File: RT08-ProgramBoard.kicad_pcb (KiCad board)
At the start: 2 copper layers, 309 parts, among them J1 PWR/Addr, J2 Instruction, J3 Data, J4 Instruction, J5 Data

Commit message: Moved a bit, updated things.csv
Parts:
- moved C10 1.27 mm to (99.1, 99.1)
- moved C11 1.27 mm to (144.8, 99.1)
- moved C12 1.27 mm to (190.5, 99.1)
- moved C14 1.27 mm to (99.1, 132.1)
- moved C15 1.27 mm to (144.8, 132.1)
- moved C16 1.27 mm to (190.5, 132.1)
- moved C2 1.27 mm to (99.1, 33.0)
- moved C3 1.27 mm to (144.8, 33.0)
- moved C4 1.27 mm to (190.5, 33.0)
- moved C6 1.27 mm to (99.1, 66.0)
- moved C7 1.27 mm to (144.8, 66.0)
- moved C8 1.27 mm to (190.5, 66.0)
- moved D11 1.27 mm to (96.5, 76.2)
- moved D12 1.27 mm to (96.5, 73.7)
- moved D19 1.27 mm to (96.5, 109.2)
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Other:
- board outline added: 190.5 x 149.9 mm

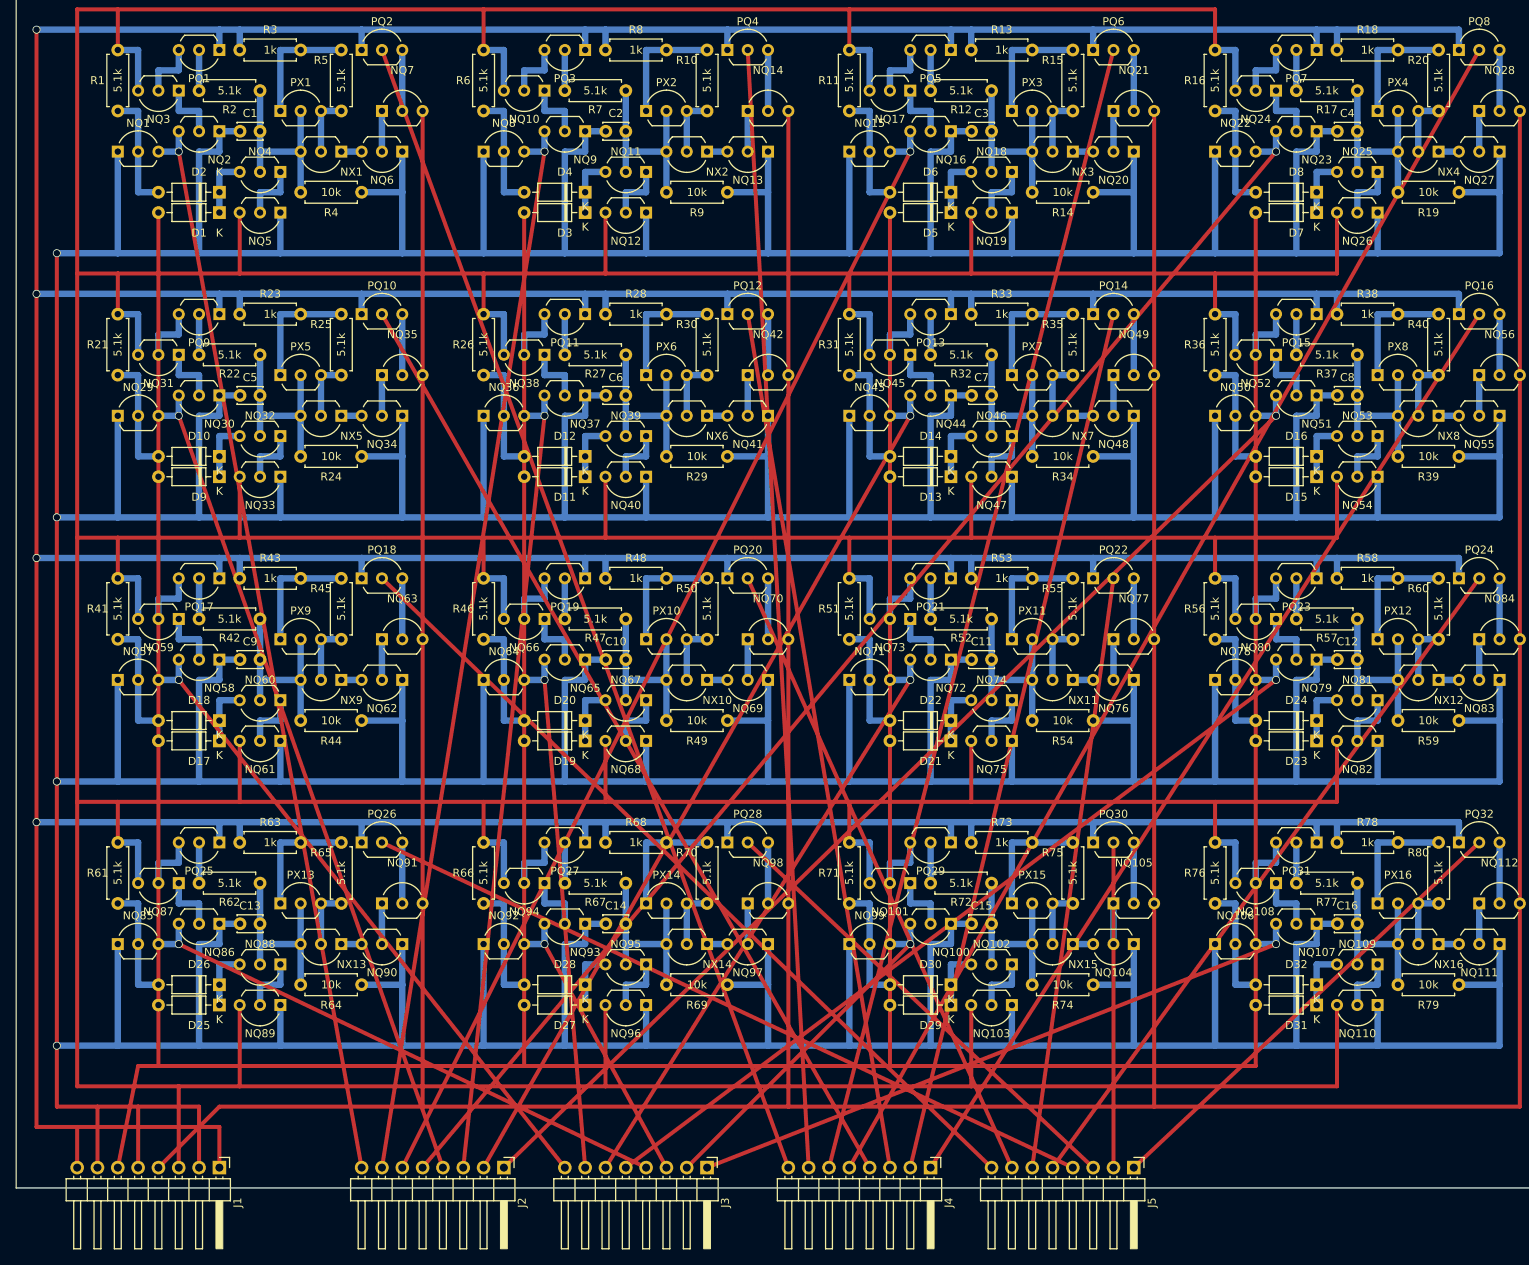
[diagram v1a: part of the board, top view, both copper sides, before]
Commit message: Deleted '-' from its name, officially
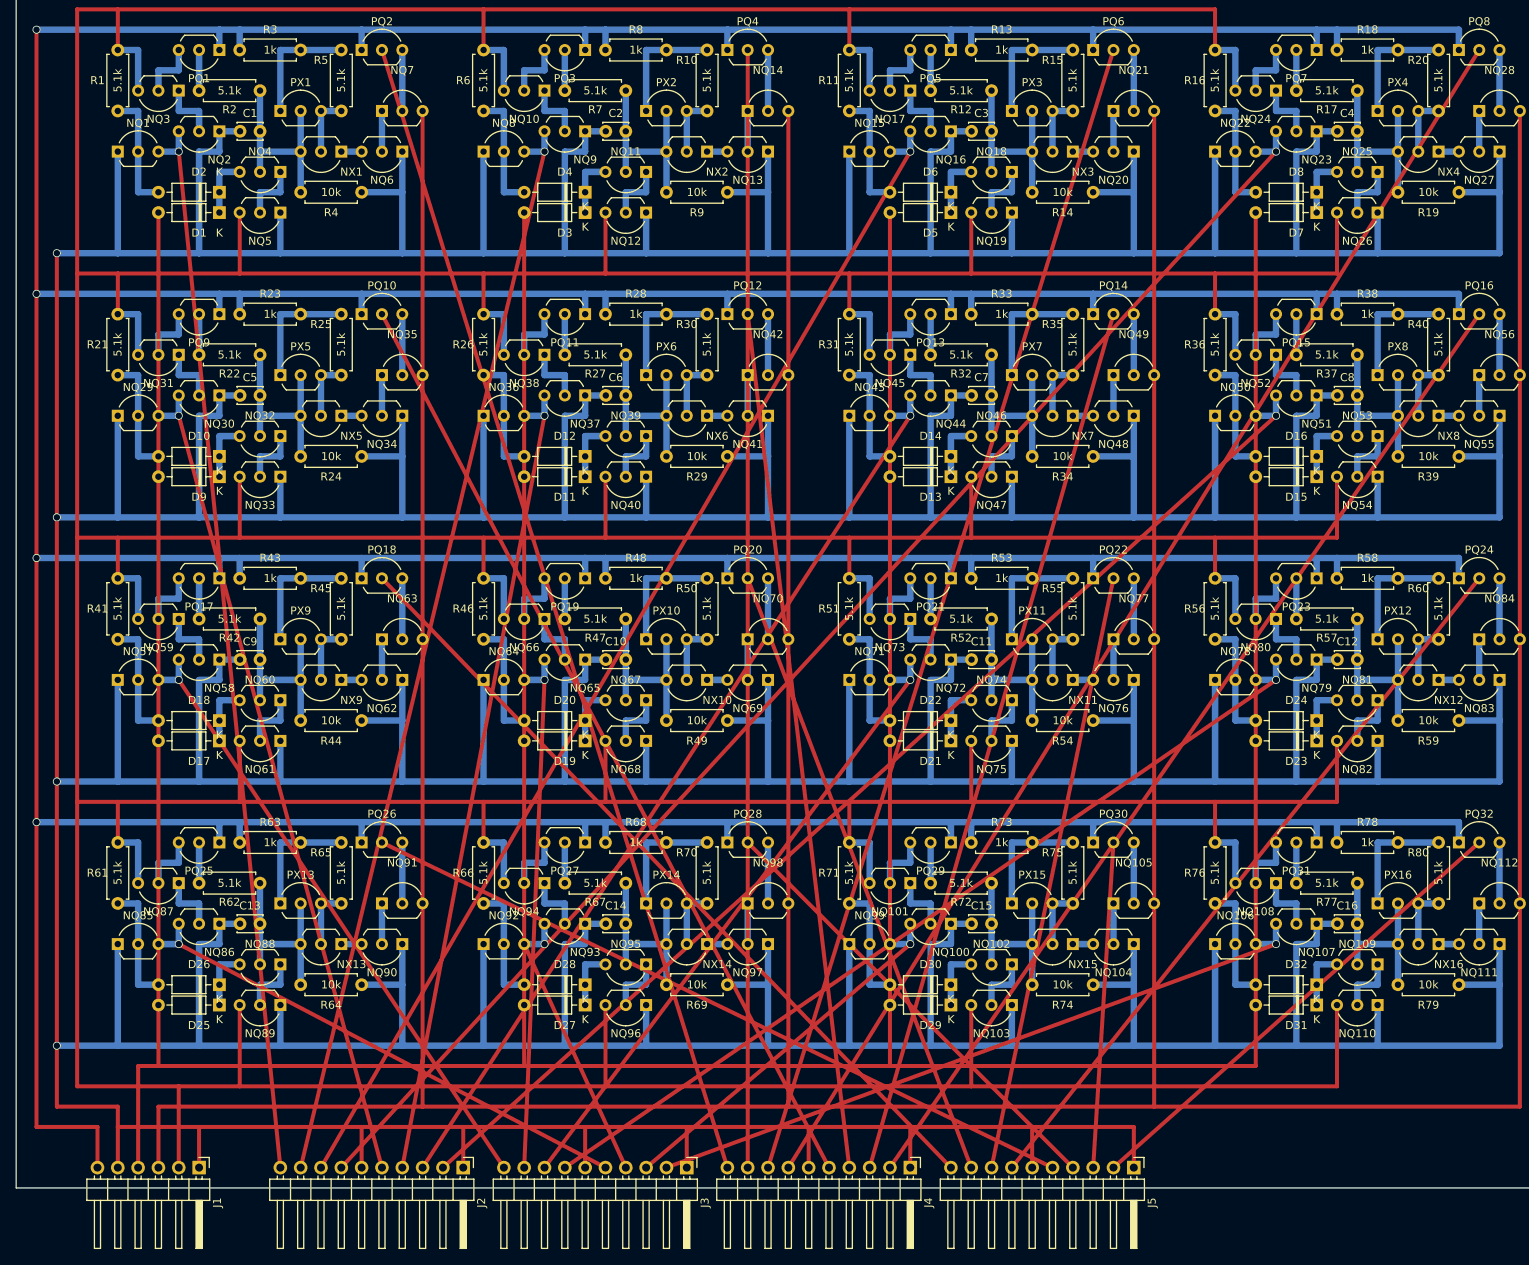
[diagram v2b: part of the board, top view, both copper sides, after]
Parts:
- D1, D10, D11, D12, D13, D14, D15, D16, D17, D18, D19, D2, D20, D21, D22, D23, D24, D25, D26, D27, D28, D29, D3, D30, D31, D32, D4, D5, D6, D7, D8, D9: value 30V0.2A -> Schottky
- J1: footprint Connector_PinHeader_2.54mm:PinHeader_1x08_P2.54mm_Horizontal -> Connector_PinHeader_2.54mm:PinHeader_1x06_P2.54mm_Horizontal
- J2, J3, J4, J5: footprint Connector_PinHeader_2.54mm:PinHeader_1x08_P2.54mm_Horizontal -> Connector_PinHeader_2.54mm:PinHeader_1x10_P2.54mm_Horizontal
- NQ103, NQ110, NQ12, NQ19, NQ26, NQ33, NQ40, NQ47, NQ5, NQ54, NQ61, NQ68, NQ75, NQ82, NQ89, NQ96: value DTC143E-THT -> DTC114E-THT
- moved J2 5.08 mm to (81.3, 162.6)
- moved J3 2.54 mm to (109.2, 162.6)
- moved J1 2.54 mm to (48.3, 162.6)
- moved J4 2.54 mm to (137.2, 162.6)
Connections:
- J1 pad 1: +5V -> GND
- J1 pad 2: GND -> /WEn
- J1 pad 3: /WEn -> /DEn
- J1 pad 4: /DEn -> /Rst
- J1 pad 6: /Rst -> +5V
- J2 pad 1: /D7 -> GND
- J2 pad 2: /D6 -> /D7
- J2 pad 3: /D5 -> /D6
- J2 pad 4: /D4 -> /D5
- J2 pad 5: /D3 -> /D4
- J2 pad 6: /D2 -> GND
- J2 pad 7: /D1 -> /D3
- J2 pad 8: /D0 -> /D2
- J3 pad 1: /D15 -> GND
- J3 pad 2: /D14 -> /D15
- J3 pad 3: /D13 -> /D14
- J3 pad 4: /D12 -> /D13
- J3 pad 5: /D11 -> /D12
- J3 pad 6: /D10 -> GND
- J3 pad 7: /D9 -> /D11
- J3 pad 8: /D8 -> /D10
- J4 pad 1: /P7 -> GND
- J4 pad 2: /P6 -> /P7
- J4 pad 3: /P5 -> /P6
- J4 pad 4: /P4 -> /P5
- J4 pad 5: /P3 -> /P4
- J4 pad 6: /P2 -> GND
- J4 pad 7: /P1 -> /P3
- J4 pad 8: /P0 -> /P2
- J5 pad 1: /P15 -> GND
- J5 pad 2: /P14 -> /P15
- J5 pad 3: /P13 -> /P14
- J5 pad 4: /P12 -> /P13
- J5 pad 5: /P11 -> /P12
- J5 pad 6: /P10 -> GND
- J5 pad 7: /P9 -> /P11
- J5 pad 8: /P8 -> /P10

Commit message: Updated pinouts n' something
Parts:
- added J6: Inst-1, Connector_PinHeader_2.54mm:PinHeader_1x06_P2.54mm_Horizontal, F.Cu at (144.8, 165.1)
- added J7: Inst-2, Connector_PinHeader_2.54mm:PinHeader_1x06_P2.54mm_Horizontal, F.Cu at (162.6, 165.1)
- added J8: Data-1, Connector_PinHeader_2.54mm:PinHeader_1x06_P2.54mm_Horizontal, F.Cu at (180.3, 165.1)
- added J9: Data-2, Connector_PinHeader_2.54mm:PinHeader_1x06_P2.54mm_Horizontal, F.Cu at (198.1, 165.1)
- J2: value Instruction -> Inst-1; footprint Connector_PinHeader_2.54mm:PinHeader_1x10_P2.54mm_Horizontal -> Connector_PinHeader_2.54mm:PinHeader_1x06_P2.54mm_Horizontal
- J3: value Data -> Inst-2; footprint Connector_PinHeader_2.54mm:PinHeader_1x10_P2.54mm_Horizontal -> Connector_PinHeader_2.54mm:PinHeader_1x06_P2.54mm_Horizontal
- J4: value Instruction -> Data-1; footprint Connector_PinHeader_2.54mm:PinHeader_1x10_P2.54mm_Horizontal -> Connector_PinHeader_2.54mm:PinHeader_1x06_P2.54mm_Horizontal
- J5: value Data -> Data-2; footprint Connector_PinHeader_2.54mm:PinHeader_1x10_P2.54mm_Horizontal -> Connector_PinHeader_2.54mm:PinHeader_1x06_P2.54mm_Horizontal
- R1, R10, R11, R12, R13, R14, R15, R16, R17, R18, R19, R2, R20, R21, R22, R23, R24, R25, R26, R27, R28, R29, R3, R30, R31, R32, R33, R34, R35, R36, R37, R38, R39, R4, R40, R41, R42, R43, R44, R45, R46, R47, R48, R49, R5, R50, R51, R52, R53, R54, R55, R56, R57, R58, R59, R6, R60, R61, R62, R63, R64, R65, R66, R67, R68, R69, R7, R70, R71, R72, R73, R74, R75, R76, R77, R78, R79, R8, R80, R9: footprint YoshLibrary:R_Axial_DIN0207_L6.3mm_D2.5mm_P7.62mm_Horizontal -> YoshLibrary:R_Axial_DIN0207_L6.3mm_D2.5mm_P7.62mm_Horizontal_Y
- moved J5 40.7 mm to (124.5, 165.1)
- moved J4 30.6 mm to (106.7, 165.1)
- moved J3 20.5 mm to (88.9, 165.1)
- moved J2 10.5 mm to (71.1, 165.1)
- moved R75 3.59 mm to (160.0, 132.1)
- moved R80 3.59 mm to (205.7, 132.1)
- moved D26 3.59 mm to (53.3, 142.2)
- moved D28 3.59 mm to (99.1, 142.2)
- moved NQ43 3.59 mm to (132.1, 71.1)
- moved NQ50 3.59 mm to (177.8, 71.1)
- moved NQ55 3.59 mm to (213.4, 71.1)
- moved NQ71 3.59 mm to (132.1, 104.1)
- moved NQ78 3.59 mm to (177.8, 104.1)
- moved NQ83 3.59 mm to (213.4, 104.1)
- moved NX11 3.59 mm to (160.0, 104.1)
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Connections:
- J2 pad 2: /D7 -> /D3
- J2 pad 3: /D6 -> /D2
- J2 pad 4: /D5 -> GND
- J2 pad 5: /D4 -> /D1
- J2 pad 6: GND -> /D0
- J3 pad 2: /D15 -> /D7
- J3 pad 3: /D14 -> /D6
- J3 pad 4: /D13 -> GND
- J3 pad 5: /D12 -> /D5
- J3 pad 6: GND -> /D4
- J4 pad 2: /P7 -> /D11
- J4 pad 3: /P6 -> /D10
- J4 pad 4: /P5 -> GND
- J4 pad 5: /P4 -> /D9
- J4 pad 6: GND -> /D8
- J5 pad 2: /P15 -> /D15
- J5 pad 3: /P14 -> /D14
- J5 pad 4: /P13 -> GND
- J5 pad 5: /P12 -> /D13
- J5 pad 6: GND -> /D12

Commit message: Changed pinheaders
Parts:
- J1, J2, J3, J4, J5, J6, J7, J8, J9: footprint Connector_PinHeader_2.54mm:PinHeader_1x06_P2.54mm_Horizontal -> Connector_PinHeader_2.54mm:PinHeader_1x06_P2.54mm_Vertical
